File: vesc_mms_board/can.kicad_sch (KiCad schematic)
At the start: 14 parts, among them J1 RJ45_LED_Shielded, J2 RJ45_LED_Shielded, J5 Conn_01x03, SW1 SW_DIP_x02

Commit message: pcb created
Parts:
- removed J5: Conn_01x03, Connector_PinHeader_2.54mm:PinHeader_1x03_P2.54mm_Vertical, symbol Connector_Generic:Conn_01x03
- added J7: Conn_01x04, Connector_PinHeader_2.54mm:PinHeader_1x04_P2.54mm_Vertical, symbol Connector_Generic:Conn_01x04
- renumbered C4 to C2, R7 to R1, R1 to R2, R2 to R3, R10 to R4, R11 to R5, R12 to R6, R13 to R7, R14 to R8
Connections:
- net CAN+: now also J7.2 (Pin_2)
- net CAN-: now also J7.3 (Pin_3)
- net GND: now also J7.4 (Pin_4)
- new net +5V: J7.1 (Pin_1)

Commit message: cehnaged leyour added vias
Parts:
- removed C1, C2: 10n, Capacitor_SMD:C_0402_1005Metric, symbol Device:C
- removed R1, R4: 33k, Resistor_SMD:R_0402_1005Metric, symbol Device:R
- added R17, R18: 1k, Resistor_SMD:R_0402_1005Metric, symbol Device:R
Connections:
- net +12V: now also R17.1, R18.1
- net GND: now also J1.11, J1.SH, J2.9, J2.SH
- net USB_UPSTREAM_D+: now also J1.8; no longer J1.7
- net USB_UPSTREAM_D-: now also J1.7; no longer J1.8
- net at J2.10: now also R17.2
- net at J1.12: now also R18.2
- no-connect marks 8 -> 4
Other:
- note removed: "min 200V"

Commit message: Update rev 2.0, added step files
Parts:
- removed J7: Conn_01x04, Connector_PinHeader_2.54mm:PinHeader_1x04_P2.54mm_Vertical, symbol Connector_Generic:Conn_01x04
- added J3: Conn_01x04, Connector_JST:JST_XH_B4B-XH-A_1x04_P2.50mm_Vertical, symbol Connector_Generic:Conn_01x04
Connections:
- net +5V: now also J3.4 (Pin_4)
- net CAN+: now also J3.3 (Pin_3)
- net CAN-: now also J3.2 (Pin_2)
- net GND: now also J3.1 (Pin_1)
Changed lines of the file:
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@@
-	)
-	(symbol
-		(lib_id "Connector_Generic:Conn_01x04")
-		(at 246.38 76.2 0)
-		(unit 1)
-		(exclude_from_sim no)
-		(in_bom yes)
-		(on_board yes)
-		(dnp no)
-		(fields_autoplaced yes)
-		(property "Reference" "J7"
-			(at 248.92 76.1999 0)
-			(effects
-				(font
-					(size 1.27 1.27)
-				)
-				(justify left)
-			)
-		)
-		(property "Value" "Conn_01x04"
-			(at 248.92 78.7399 0)
-			(effects
-				(font
-					(size 1.27 1.27)
-				)
-				(justify left)
-			)
-		)
-		(property "Footprint" "Connector_PinHeader_2.54mm:PinHeader_1x04_P2.54mm_Vertical"
-			(at 246.38 76.2 0)
-			(effects
-				(font
-					(size 1.27 1.27)
-				)
-				(hide yes)
-			)
-		)
-		(property "Datasheet" "~"
-			(at 246.38 76.2 0)
-			(effects
-				(font
-					(size 1.27 1.27)
-				)
-				(hide yes)
-			)
-		)
-		(property "Description" "Generic connector, single row, 01x04, script generated (kicad-library-utils/schlib/autogen/connector/)"
-			(at 246.38 76.2 0)
-			(effects
-				(font
-					(size 1.27 1.27)
-				)
-				(hide yes)
-			)
-		)
-		(pin "2"
-		)
-		(pin "1"
-		)
-		(pin "3"
-		)
-		(pin "4"
-		)
-		(instances
-			(project ""
-				(path "/19c3ad7a-1b7d-4298-9053-cf734bfcea10/57d5ea5a-77df-43d7-95b9-bf9fc02879bb"
-					(reference "J7")
-					(unit 1)
-				)
-			)
-		)
 	)
 	(symbol
@@
 					(unit 1)
 				)
+			)
+		)
+	)
+	(symbol
+		(lib_id "Connector_Generic:Conn_01x04")
+		(at 246.38 78.74 0)
+		(mirror x)
+		(unit 1)
+		(exclude_from_sim no)
+		(in_bom yes)
+		(on_board yes)
+		(dnp no)
+		(property "Reference" "J3"
+			(at 248.92 78.7401 0)
+			(effects
+				(font
+					(size 1.27 1.27)
+				)
+				(justify left)
+			)
+		)
+		(property "Value" "Conn_01x04"
+			(at 248.92 76.2001 0)
+			(effects
+				(font
+					(size 1.27 1.27)
+				)
+				(justify left)
+			)
+		)
+		(property "Footprint" "Connector_JST:JST_XH_B4B-XH-A_1x04_P2.50mm_Vertical"
+			(at 246.38 78.74 0)
+			(effects
+				(font
+					(size 1.27 1.27)
+				)
+				(hide yes)
+			)
+		)
+		(property "Datasheet" "~"
+			(at 246.38 78.74 0)
+			(effects
+				(font
+					(size 1.27 1.27)
+				)
+				(hide yes)
+			)
+		)
+		(property "Description" "Generic connector, single row, 01x04, script generated (kicad-library-utils/schlib/autogen/connector/)"
+			(at 246.38 78.74 0)
+			(effects
+				(font
+					(size 1.27 1.27)
+				)
+				(hide yes)
+			)
+		)
+		(pin "2"
+		)
+		(pin "1"
+		)
+		(pin "3"
+		)
+		(pin "4"
+		)
+		(instances
+			(project "vesc_mms_board"
+				(path "/19c3ad7a-1b7d-4298-9053-cf734bfcea10/57d5ea5a-77df-43d7-95b9-bf9fc02879bb"
+					(reference "J3")
+					(unit 1)
+				)

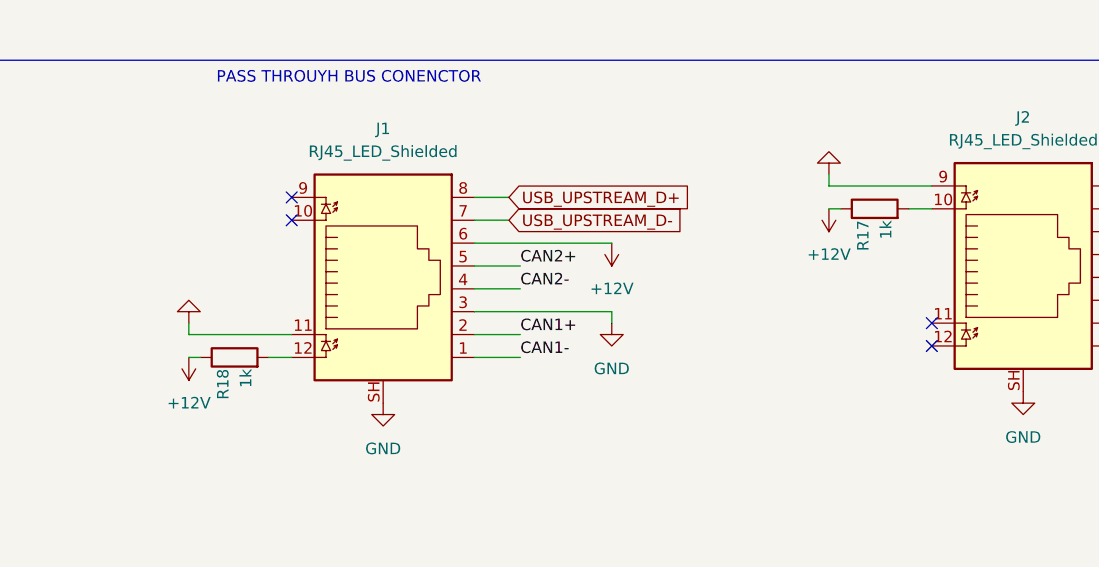
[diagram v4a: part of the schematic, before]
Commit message: fixed xt60 connvetor
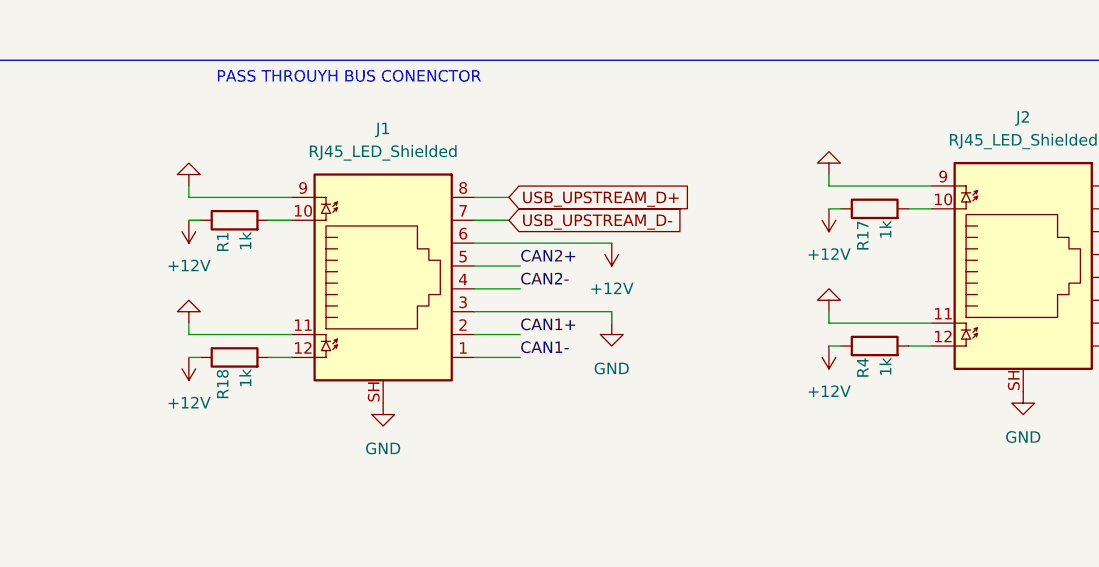
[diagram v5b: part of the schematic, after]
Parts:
- added R1, R4: 1k, Resistor_SMD:R_0402_1005Metric, symbol Device:R
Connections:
- net +12V: now also R1.1, R4.1
- net GND: now also J1.9, J2.11
- net at J2.12: now also R4.2
- net at J1.10: now also R1.2
- no-connect marks 4 -> 0
